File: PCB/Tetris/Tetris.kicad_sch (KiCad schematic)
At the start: 49 parts, among them J1 Power, J2 PWM, J3 Analog, J4 PWM, J5 Analog, J6 Communication, J7 Digital, M1 RGBMatrix, M2 RGBMatrix, SW1 SW_Push, SW2 SW_Push, SW3 SW_Push, SW4 SW_Push, SW5 SW_Push, SW6 SW_Push, SW7 SW_Push, U1 74HC595, U2 74HC595

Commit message: sync hcnages
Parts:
- removed U2: 74HC595, Package_DIP:DIP-16_W7.62mm_Socket_LongPads, symbol 74xx:74HC595
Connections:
- net S10 is gone; now on net *8: M2.10 (R_2)
- net S11 is gone; now on net *7: M2.11 (R_3)
- net S12 is gone; now on net *6: M2.12 (R_4)
- net S13 is gone; now on net *5: M2.13 (R_5)
- net S14 is gone; now on net *4: M2.14 (R_6)
- net S15 is gone; now on net *3: M2.15 (R_7)
- net S16 is gone; now on net *2: M2.16 (R_8)
- net S9 is gone; now on net *9: M2.9 (R_1)
- net *10: no longer BZ4.1 (-)
- net *11: no longer BZ3.1 (-)
- net *12: no longer BZ2.1 (-)
- net *13: no longer BZ1.1 (-)
- net *2: now also M1.16 (R_8), M1.28 (G_1), M1.8 (B_8), M2.8 (B_8)
- net *3: now also M1.15 (R_7), M1.27 (G_2), M1.7 (B_7), M2.7 (B_7)
- net *4: now also M1.14 (R_6), M1.26 (G_3), M1.6 (B_6), M2.6 (B_6)
- net *5: now also M1.13 (R_5), M1.25 (G_4), M1.5 (B_5), M2.5 (B_5)
- net *52: no longer M1.16 (R_8)
- net *6: now also M1.12 (R_4), M1.24 (G_5), M1.4 (B_4), M2.4 (B_4)
- net *7: now also M1.11 (R_3), M1.23 (G_6), M1.3 (B_3), M2.3 (B_3)
- net *8: now also M1.10 (R_2), M1.2 (B_2), M1.22 (G_7), M2.2 (B_2)
- net *9: now also M1.1 (B_1), M1.21 (G_8), M1.9 (R_1), M2.1 (B_1)
- net A0: no longer M1.1 (B_1)
- net A1: no longer M1.2 (B_2)
- net A10: no longer M1.11 (R_3)
- net A11: no longer M1.12 (R_4)
- net A12: no longer M1.13 (R_5)
- net A13: no longer M1.14 (R_6)
- net A14: no longer M1.15 (R_7)
- net A2: no longer M1.3 (B_3)
- net A3: no longer M1.4 (B_4)
- net A4: no longer M1.5 (B_5)
- net A5: no longer M1.6 (B_6)
- net A6: no longer M1.7 (B_7)
- net A7: no longer M1.8 (B_8)
- net A8: no longer M1.9 (R_1)
- net A9: no longer M1.10 (R_2)
- net RX1/19: no longer M1.23 (G_6)
- net RX2/17: no longer M1.25 (G_4)
- net RX3/15: no longer M1.27 (G_2)
- net S1: no longer M2.1 (B_1)
- net S2: no longer M2.2 (B_2)
- net S3: no longer M2.3 (B_3)
- net S4: no longer M2.4 (B_4)
- net S5: no longer M2.5 (B_5)
- net S6: no longer M2.6 (B_6)
- net S7: no longer M2.7 (B_7)
- net S8: no longer M2.8 (B_8)
- net SCL/21: no longer M1.21 (G_8)
- net SDA/20: no longer M1.22 (G_7)
- net TX1/18: no longer M1.24 (G_5)
- net TX2/16: no longer M1.26 (G_3)
- net TX3/14: no longer M1.28 (G_1)

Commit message: MASSIVE PROGRESS
Redesign PCB to use ports
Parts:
- added J8: Digital, Connector_PinHeader_2.54mm:PinHeader_2x08_P2.54mm_Vertical, symbol Connector_Generic:Conn_02x08_Odd_Even
- J1: footprint Connector_PinHeader_2.54mm:PinHeader_1x08_P2.54mm_Vertical -> Connector_PinHeader_2.54mm:PinHeader_1x02_P2.54mm_Vertical; symbol Connector_Generic:Conn_01x08 -> Connector_Generic:Conn_01x02
- J2: footprint Connector_PinHeader_2.54mm:PinHeader_1x10_P2.54mm_Vertical -> Connector_PinHeader_2.54mm:PinHeader_1x07_P2.54mm_Vertical; symbol Connector_Generic:Conn_01x10 -> Connector_Generic:Conn_01x07
- J4: footprint Connector_PinHeader_2.54mm:PinHeader_1x08_P2.54mm_Vertical -> Connector_PinHeader_2.54mm:PinHeader_1x06_P2.54mm_Vertical; symbol Connector_Generic:Conn_01x08 -> Connector_Generic:Conn_01x06
- J7: footprint Connector_PinHeader_2.54mm:PinHeader_2x18_P2.54mm_Vertical -> Connector_PinHeader_2.54mm:PinHeader_2x09_P2.54mm_Vertical; symbol Connector_Generic:Conn_02x18_Odd_Even -> Connector_Generic:Conn_02x09_Odd_Even
- R1, R10, R11, R12, R2, R24, R25, R26, R27, R3, R4, R5, R6, R7, R8, R9: footprint Resistor_THT:R_Axial_DIN0207_L6.3mm_D2.5mm_P10.16mm_Horizontal -> RGBMatrix:R_Axial_DIN0207_L6.3mm_D2.5mm_P12.40mm_Horizontal
- R17, R18: footprint Resistor_THT:R_Axial_DIN0207_L6.3mm_D2.5mm_P10.16mm_Horizontal -> Resistor_THT:R_Axial_DIN0207_L6.3mm_D2.5mm_P7.62mm_Horizontal
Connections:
- net 39 is gone; now on net +5V: J7.18 (Pin_18)
- net AREF is gone; now on net *12: J2.3 (Pin_3)
- net IOREF is gone; now on net GND: J1.2 (Pin_2)
- net RX3/15 is gone; now on net 15: J6.2 (Pin_2)
- net *10: now also J2.5 (Pin_5), M2.4 (B_4); no longer J2.8 (Pin_8)
- net *11: now also J2.4 (Pin_4), M2.3 (B_3); no longer J2.7 (Pin_7)
- net *12: now also M2.2 (B_2); no longer J2.6 (Pin_6)
- net *13: now also J2.2 (Pin_2), M2.1 (B_1); no longer J2.5 (Pin_5)
- net *2: no longer M1.16 (R_8), M1.28 (G_1), M1.8 (B_8), M2.16 (R_8), M2.28 (G_1), M2.8 (B_8)
- net *3: no longer M1.15 (R_7), M1.27 (G_2), M1.7 (B_7), M2.15 (R_7), M2.27 (G_2), M2.7 (B_7)
- net *4: now also U1.11 (SRCLK); no longer M1.14 (R_6), M1.26 (G_3), M1.6 (B_6), M2.14 (R_6), M2.26 (G_3), M2.6 (B_6)
- net *44: now also M2.11 (R_3), J8.11 (Pin_11); no longer J7.11 (Pin_11), U1.14 (SER)
- net *45: now also M2.12 (R_4), J8.12 (Pin_12); no longer J7.12 (Pin_12)
- net *46: now also M2.13 (R_5), J8.9 (Pin_9); no longer J7.9 (Pin_9)
- net *5: now also U1.12 (RCLK); no longer M1.13 (R_5), M1.25 (G_4), M1.5 (B_5), M2.13 (R_5), M2.25 (G_4), M2.5 (B_5)
- net *52: now also M2.7 (B_7), J8.3 (Pin_3); no longer J7.3 (Pin_3)
- net *6: now also BZ1.1 (-); no longer M1.12 (R_4), M1.24 (G_5), M1.4 (B_4), M2.12 (R_4), M2.24 (G_5), M2.4 (B_4)
- net *7: now also BZ2.1 (-); no longer M1.11 (R_3), M1.23 (G_6), M1.3 (B_3), M2.11 (R_3), M2.23 (G_6), M2.3 (B_3)
- net *8: now also BZ3.1 (-), J2.7 (Pin_7); no longer J2.10 (Pin_10), M1.10 (R_2), M1.2 (B_2), M1.22 (G_7), M2.10 (R_2), M2.2 (B_2), M2.22 (G_7)
- net *9: now also BZ4.1 (-), J2.6 (Pin_6); no longer J2.9 (Pin_9), M1.1 (B_1), M1.21 (G_8), M1.9 (R_1), M2.1 (B_1), M2.21 (G_8), M2.9 (R_1)
- net +5V: now also J1.1 (Pin_1), J7.17 (Pin_17); no longer J1.5 (Pin_5), J7.35 (Pin_35), J7.36 (Pin_36)
- net 22: now also J7.15 (Pin_15), M1.21 (G_8); no longer J7.33 (Pin_33)
- net 23: now also J7.16 (Pin_16), M1.22 (G_7); no longer J7.34 (Pin_34), R17.2, SW1.1
- net 24: now also J7.13 (Pin_13), M1.23 (G_6); no longer J7.31 (Pin_31), R12.1, R4.1
- net 25: now also J7.14 (Pin_14), M1.24 (G_5); no longer J7.32 (Pin_32), R23.1, SW7.1
- net 26: now also J7.11 (Pin_11), M1.25 (G_4); no longer J7.29 (Pin_29), R11.1, R3.1
- net 27: now also J7.12 (Pin_12), M1.26 (G_3); no longer J7.30 (Pin_30), R18.2, SW2.1
- net 28: now also J7.9 (Pin_9), M1.27 (G_2); no longer J7.27 (Pin_27), R10.1, R2.1
- net 29: now also J7.10 (Pin_10), M1.28 (G_1); no longer J7.28 (Pin_28)
- net 30: now also J7.7 (Pin_7), M2.28 (G_1); no longer J7.25 (Pin_25), R1.1, R9.1
- net 31: now also J7.8 (Pin_8), M2.27 (G_2); no longer J7.26 (Pin_26), R19.2, SW3.1
- net 32: now also J7.5 (Pin_5), M2.26 (G_3); no longer J7.23 (Pin_23), R13.2, R5.2
- net 33: now also J7.6 (Pin_6), M2.25 (G_4); no longer J7.24 (Pin_24), R21.2, SW5.1
- net 34: now also J7.3 (Pin_3), M2.24 (G_5); no longer J7.21 (Pin_21), R14.2, R6.2
- net 35: now also J7.4 (Pin_4), M2.23 (G_6); no longer J7.22 (Pin_22)
- net 36: now also J7.1 (Pin_1), M2.22 (G_7); no longer J7.19 (Pin_19), R15.2, R7.2
- net 37: now also J7.2 (Pin_2), M2.21 (G_8); no longer J7.20 (Pin_20), R22.1, SW6.1
- net 40: now also U1.14 (SER), J8.15 (Pin_15); no longer J7.15 (Pin_15), U1.12 (RCLK)
- net 42: now also M2.9 (R_1), J8.13 (Pin_13); no longer J7.13 (Pin_13), U1.11 (SRCLK)
- net 43: now also M2.10 (R_2), J8.14 (Pin_14); no longer J7.14 (Pin_14)
- net 47: now also M2.14 (R_6), J8.10 (Pin_10); no longer J7.10 (Pin_10)
- net 48: now also M2.15 (R_7), J8.7 (Pin_7); no longer J7.7 (Pin_7)
- net 49: now also M2.16 (R_8), J8.8 (Pin_8); no longer J7.8 (Pin_8)
- net 50: now also M2.5 (B_5), J8.5 (Pin_5); no longer J7.5 (Pin_5)
- net 51: now also M2.6 (B_6), J8.6 (Pin_6); no longer J7.6 (Pin_6)
- net 53: now also M2.8 (B_8), J8.4 (Pin_4); no longer J7.4 (Pin_4)
- net A0: now also M1.1 (B_1)
- net A1: now also M1.2 (B_2)
- net A10: now also M1.11 (R_3)
- net A11: now also M1.12 (R_4)
- net A12: now also M1.13 (R_5)
- net A13: now also M1.14 (R_6)
- net A14: now also M1.15 (R_7)
- net A15: now also M1.16 (R_8)
- net A2: now also M1.3 (B_3)
- net A3: now also M1.4 (B_4)
- net A4: now also M1.5 (B_5)
- net A5: now also M1.6 (B_6)
- net A6: now also M1.7 (B_7)
- net A7: now also M1.8 (B_8)
- net A8: now also M1.9 (R_1)
- net A9: now also M1.10 (R_2)
- net GND: now also J2.1 (Pin_1), J8.1 (Pin_1), J8.2 (Pin_2); no longer J1.6 (Pin_6), J1.7 (Pin_7), J2.4 (Pin_4), J7.1 (Pin_1), J7.2 (Pin_2)
- net S1: now also R1.1, R9.1
- net S2: now also R10.1, R2.1
- net S3: now also R11.1, R3.1
- net S4: now also R12.1, R4.1
- net S5: now also R13.2, R5.2
- net S6: now also R14.2, R6.2
- net S7: now also R15.2, R7.2
- net S8: now also R16.2, R8.2
- removed net +3V3: J1.4 (Pin_4)
- removed net 38: J7.17 (Pin_17), R16.2, R8.2
- net 41 renamed 15
- net 15: no longer J7.16 (Pin_16)
- removed net RX0/0: J4.8 (Pin_8)
- net RX1/19 renamed 19
- net 19: now also R17.2, SW1.1
- net RX2/17 renamed 17
- net 17: now also R22.1, SW6.1
- net SCL/21 renamed 21
- net 21: now also R23.1, SW7.1; no longer J2.1 (Pin_1)
- net SDA/20 renamed 20
- net 20: now also R18.2, SW2.1; no longer J2.2 (Pin_2)
- removed net TX0/1: J4.7 (Pin_7)
- net TX1/18 renamed 18
- net 18: now also R19.2, SW3.1
- net TX2/16 renamed 16
- net 16: now also R21.2, SW5.1
- net TX3/14 renamed 14
- removed net VCC: J1.8 (Pin_8)
- removed net ~{RESET}: J1.3 (Pin_3)
- no-connect marks 1 -> 0
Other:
- moved on the sheet: J3, J5, J6

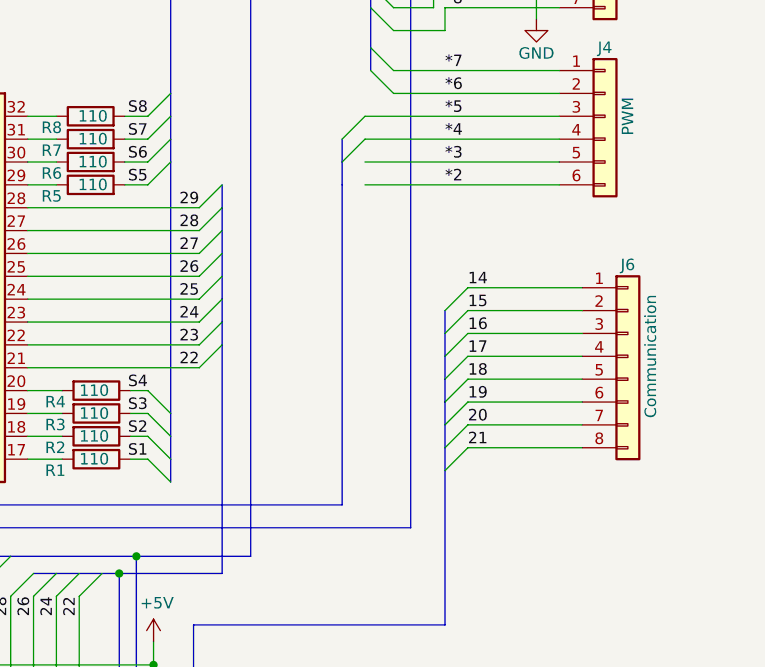
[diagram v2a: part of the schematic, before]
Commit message: Cleaned up and tidy repository
Removed duplicated/unwanted PCB files,

Added pictures for read me
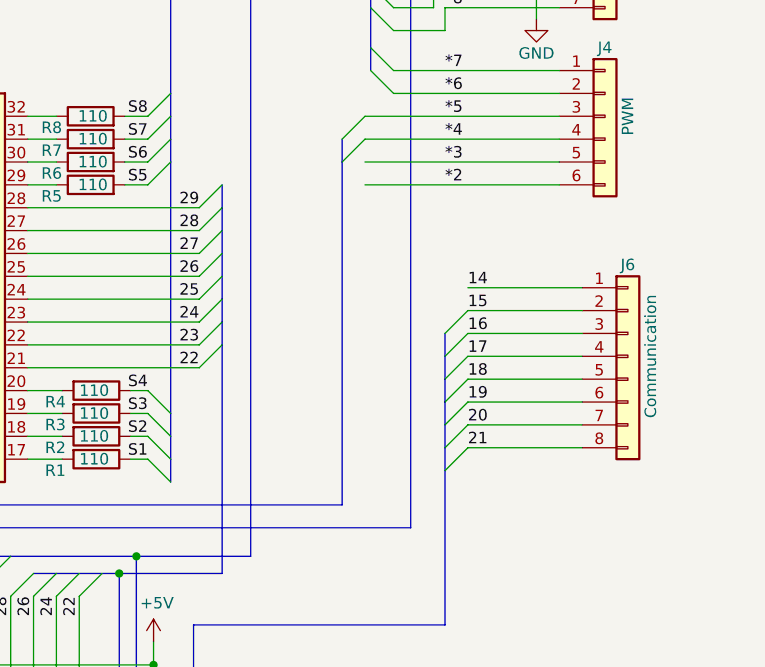
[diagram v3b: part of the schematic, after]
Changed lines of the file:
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@@
-    (stroke (width 0) (type default))
-  )
-  (bus_entry (at 205.105 114.3) (size -2.54 2.54)
     (stroke (width 0) (type default))
   )
@@
     (stroke (width 0) (type default))
   )
-  (bus (pts (xy 202.565 116.84) (xy 202.565 119.38))
-    (stroke (width 0) (type default))
-  )
   (wire (pts (xy 114.935 154.305) (xy 114.935 158.75))
     (stroke (width 0) (type default))
@@
     (stroke (width 0) (type default))
   )
-  (bus (pts (xy 191.135 100.33) (xy 191.135 102.87))
+  (bus (pts (xy 191.135 100.33) (xy 191.135 138.43))
     (stroke (width 0) (type default))
   )
@@
     (stroke (width 0) (type default))
   )
-  (bus (pts (xy 191.135 102.87) (xy 191.135 138.43))
-    (stroke (width 0) (type default))
-  )
